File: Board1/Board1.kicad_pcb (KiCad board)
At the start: 2 copper layers, 100 x 62 mm, 60 parts, among them J1 240VAC, J2 PTC Plate, J3 Thermo, J4 Cool. Plate, J5 OLED, J6 Rotary Encoder, J7 ESPFlash, J8 Fan, J9 IR Therm, Q1 2N7002E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

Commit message: Resolve library and ERC issues
No changes to design.
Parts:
- U4: footprint Relay_THT:SSR_AQG22105 -> 0_Project:SSR_AQG22105
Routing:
- net GND: track 42.6 -> 43.9 mm, vias 33 -> 34
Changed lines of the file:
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@@
 	)
 	(paper "A4")
+	(title_block
+		(title "Board 1 (Reflow Controller)")
+		(date "2025-02-20")
+		(rev "1.1")
+		(company "Wattle Labs")
+	)
 	(layers
 		(0 "F.Cu" signal "Front")
@@
 	(net 52 "unconnected-(U1-IO37-Pad30)")
 	(net 53 "unconnected-(U1-IO4-Pad4)")
-	(net 54 "unconnected-(U3-DNC-Pad8)")
+	(net 54 "unconnected-(U3-NC-Pad8)")
 	(net 55 "unconnected-(U1-IO38-Pad31)")
 	(net 56 "unconnected-(U1-IO3-Pad15)")
@@
 			)
 		)
-		(property "Description" "Cold Junction K-type Termocouple Interface, SPI, SO8"
+		(property "Description" "Cold Junction K-type Thermocouple Interface, SPI, SOIC-8"
 			(at 0 0 0)
 			(layer "F.Fab")
@@
 			)
 		)
-		(property "Supplier" "https://www.digikey.co.nz/en/products/detail/analog-devices-inc-maxim-integrated/MAX31855KASA/2591564"
+		(property "Supplier" ""
 			(at 0 0 0)
 			(unlocked yes)
@@
 			)
 		)
-		(property "Digikey_PN" "MAX31855KASA+-ND"
+		(property "Digikey_PN" ""
 			(at 0 0 0)
 			(unlocked yes)
@@
 			(roundrect_rratio 0.25)
 			(net 33 "+3.3V")
-			(pinfunction "V_CC")
+			(pinfunction "V_{CC}")
 			(pintype "power_in")
 		)
@@
 			(layers "F.Cu" "F.Paste" "F.Mask")
 			(roundrect_rratio 0.25)
-			(net 54 "unconnected-(U3-DNC-Pad8)")
-			(pinfunction "DNC")
-			(pintype "passive+no_connect")
+			(net 54 "unconnected-(U3-NC-Pad8)")
+			(pinfunction "NC")
+			(pintype "no_connect")
 		)
 		(model "${KICAD8_3DMODEL_DIR}/Package_SO.3dshapes/SOIC-8_3.9x4.9mm_P1.27mm.wrl"
@@
 			(net 0)
 			(net_name "")
-			(layers "F&B.Cu")
+			(layers "F.Cu" "B.Cu")
 			(hatch full 0.508)
 			(connect_pads
@@
 		)
 	)
-	(footprint "Relay_THT:SSR_AQG22105"
+	(footprint "0_Project:SSR_AQG22105"
 		(layer "F.Cu")
 		(at 55.2 55.4 180)
 		(property "Reference" "U4"
-			(at 11.5 -3.5 0)
+			(at 11.5 -3.6 180)
 			(layer "F.SilkS")
 			(effects
@@
 		)
 		(property "Value" "AQG22205"
-			(at -3.61 4.135 0)
+			(at -3.61 4.135 180)
 			(layer "F.Fab")
 			(effects
@@
 			)
 		)
-		(property "Footprint" "Relay_THT:SSR_AQG22105"
-			(at 0 0 0)
+		(property "Footprint" "0_Project:SSR_AQG22105"
+			(at 0 0 180)
 			(layer "F.Fab")
 			(hide yes)
@@
 		)
 		(property "Datasheet" ""
-			(at 0 0 0)
+			(at 0 0 180)
 			(layer "F.Fab")
 			(hide yes)
@@
 		)
 		(property "Description" "SSR RELAY SPST-NO 2A 75-264V"
-			(at 0 0 0)
+			(at 0 0 180)
 			(layer "F.Fab")
 			(hide yes)
@@
 			(solder_mask_margin 0.102)
 		)
-		(model "${KIPRJMOD}/Library/3DModels/SSR_AQG22105.step"
-			(offset
-				(xyz 0 0 0)
-			)
-			(scale
-				(xyz 1 1 1)
-			)
-			(rotate
-				(xyz -90 0 0)
-			)
-		)
 	)
 	(footprint "Button_Switch_SMD:SW_SPST_PTS810"
@@
 			)
 		)
-		(property "Datasheet" "http://www.apem.com/int/index.php?controller=attachment&id_attachment=1371"
+		(property "Datasheet" "https://www.ckswitches.com/media/1476/pts810.pdf"
 			(at 0 0 180)
 			(unlocked yes)
@@
 			)
 		)
-		(property "Datasheet" "http://www.apem.com/int/index.php?controller=attachment&id_attachment=1371"
+		(property "Datasheet" "https://www.ckswitches.com/media/1476/pts810.pdf"
 			(at 0 0 180)
 			(unlocked yes)
@@
 		(attr through_hole)
 		(fp_line
-			(start -3.23 -3.38)
-			(end -3.23 33.860001)
+			(start 21.01 -3.38)
+			(end -3.23 -3.38)
 			(stroke
 				(width 0.12)
@@
 		)
 		(fp_line
-			(start 21.01 -3.379999)
-			(end -3.23 -3.38)
+			(start 21.01 -3.38)
+			(end 21.01 33.86)
 			(stroke
 				(width 0.12)
@@
 		)
 		(fp_line
-			(start 21.01 -3.379999)
-			(end 21.01 33.86)
+			(start -3.23 -3.38)
+			(end -3.23 33.86)
 			(stroke
 				(width 0.12)
@@
 		(fp_line
 			(start -3.61 -2)
-			(end -3.61 4.000001)
+			(end -3.61 4)
 			(stroke
 				(width 0.12)
@@
 		)
 		(fp_line
-			(start -3.23 33.860001)
+			(start -3.23 33.86)
 			(end 21.01 33.86)
 			(stroke
@@
 		)
 		(pad "3" thru_hole circle
-			(at 0 5.079999 90)
+			(at 0 5.08 90)
 			(size 2.3 2.3)
 			(drill 0.8)
@@
 	)
 	(segment
+		(start 118.575 78.825)
+		(end 118.55 78.85)
+		(width 0.2)
+		(layer "F.Cu")
+		(net 3)
+	)
+	(segment
+		(start 118.575 77.525)
+		(end 118.575 78.825)
+		(width 0.2)
+		(layer "F.Cu")
+		(net 3)
+	)
+	(segment
 		(start 123.35 46.6)
 		(end 123.35 48.35)
@@
 	)
 	(via
+		(at 118.55 78.85)
+		(size 0.6)
+		(drill 0.3)
+		(layers "F.Cu" "B.Cu")
+		(net 3)
+	)
+	(via
 		(at 73.75 55.331249)
 		(size 0.6)
@@
 		(net 32)
 		(net_name "+5V")
-		(layers "F&B.Cu")
+		(layers "F.Cu" "B.Cu")
 		(hatch edge 0.5)
 		(priority 1)
@@
 		(net 33)
 		(net_name "+3.3V")
-		(layers "F&B.Cu")
+		(layers "F.Cu" "B.Cu")
 		(hatch edge 0.5)
 		(priority 3)
@@
 		(net 3)
 		(net_name "GND")
-		(layers "F&B.Cu")
+		(layers "F.Cu" "B.Cu")
 		(hatch edge 0.5)
 		(priority 2)

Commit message: v1.2 release of board with bug fixes etc
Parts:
- removed C10: 10n, Capacitor_SMD:C_0603_1608Metric
- removed D2: 1N4148, Diode_SMD:Nexperia_CFP3_SOD-123W
- removed D3: SS15, Diode_SMD:D_SMA
- removed FB1, FB2: 470R 1LN, Resistor_SMD:R_0603_1608Metric
- removed J3: Thermo, Connector_PinHeader_2.54mm:PinHeader_1x02_P2.54mm_Vertical
- removed Q2: DMN3010LK3, Package_TO_SOT_SMD:TO-252-2
- removed R15: 4k7, Resistor_SMD:R_0603_1608Metric_Pad0.98x0.95mm_HandSolder
- removed R7, R8: 220R, Resistor_SMD:R_0603_1608Metric_Pad0.98x0.95mm_HandSolder
- removed R9: 10k, Resistor_SMD:R_0603_1608Metric_Pad0.98x0.95mm_HandSolder
- removed U5: VOS615A-1X001T, Package_SO:SSOP-4_4.4x2.6mm_P1.27mm
- added D4: SS15, Diode_SMD:D_SMA, F.Cu at (63.8, 71.6)
- added R12: 300, Resistor_SMD:R_0603_1608Metric, F.Cu at (92.0, 57.0)
- added U6: DMN3010LK3-13, Wattle_Mosfets:TO252-3L_DIO, F.Cu at (81.5, 54.5)
- C6: value 10u -> 22u
- C9: value 100n -> 0.1u
- J2: footprint TerminalBlock_Altech:Altech_AK100_1x02_P5.00mm -> TerminalBlock_Altech:Altech_AK100_1x03_P5.00mm
- J4: value Cool. Plate -> Cool.Plate
- J6: value Rotary Encoder -> Rot.Encoder
- J9: value IR Therm -> IRTherm
- U3: value MAX31855KASA -> DGD0280WT-7; footprint Package_SO:SOIC-8_3.9x4.9mm_P1.27mm -> Wattle_Mosfet_Drv:SOT23-5_INF
- U4: value AQG22205 -> AQG22105
- moved C9 17.8 mm to (96.8, 53.5), turned to 90 degrees
- moved U3 14.2 mm to (93.2, 53.0), turned to 180 degrees
- moved J2 5.00 mm to (37.2, 74.2)
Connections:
- C9 pad 1: +3.3V -> +5V
- J6 pad 3: ROTARY_SIG -> ROTARY_BTN
- J6 pad 5: ROTARY_BTN -> ROTARY_SIG
- U1 pad 20: THERMO_MISO -> unconnected-(U1-IO12-Pad20)
- U1 pad 21: THERMO_CS -> unconnected-(U1-IO13-Pad21)
- U1 pad 22: THERMO_SCK -> unconnected-(U1-IO14-Pad22)
- U1 pad 23: ROTARY_SIG -> ROTARY_BTN
- U1 pad 25: ROTARY_BTN -> ROTARY_SIG
- U3 pad 1: GND -> +5V
- U3 pad 2: Net-(U3-T-) -> GND
- U3 pad 3: Net-(U3-T+) -> FAN
- U3 pad 4: +3.3V -> unconnected-(U3-3V3-Pad4)
- U3 pad 5: THERMO_SCK -> Net-(U3-OUT)
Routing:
- net +5V: track 121.0 -> 133.4 mm
- net THERMO_SCK: track 10.0 -> 0.00 mm
- net THERMO_MISO: track 10.0 -> 0.00 mm
- net THERMO_CS: track 10.0 -> 0.00 mm
- net GND: track 43.9 -> 37.3 mm
- net +3.3V: track 133.9 -> 127.5 mm, vias 17 -> 16
- net ROTARY_BTN: track 28.3 -> 34.4 mm
- net ROTARY_SIG: track 34.4 -> 28.3 mm
- net Net-(D2-K): track 5.46 -> 0.00 mm
- net Net-(Q2-G): track 5.23 -> 0.00 mm
- net Net-(U3-T+): track 4.74 -> 0.00 mm
- net Net-(J2-Pin_1): track 22.5 -> 27.2 mm
- net Net-(U3-T-): track 4.62 -> 0.00 mm
- net Net-(U6-G): track 0.00 -> 4.38 mm
- net Net-(R7-Pad1): track 3.56 -> 0.00 mm
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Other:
- outline, holes or cut-outs redrawn
- board text added: "2025/03 - v1.2"
- board text added: "YAORP^{32}"
- board text removed: "2025/02 - v1.1"
- board text removed: "T+"
- board text removed: "T-"
- board text removed: "YAORP"

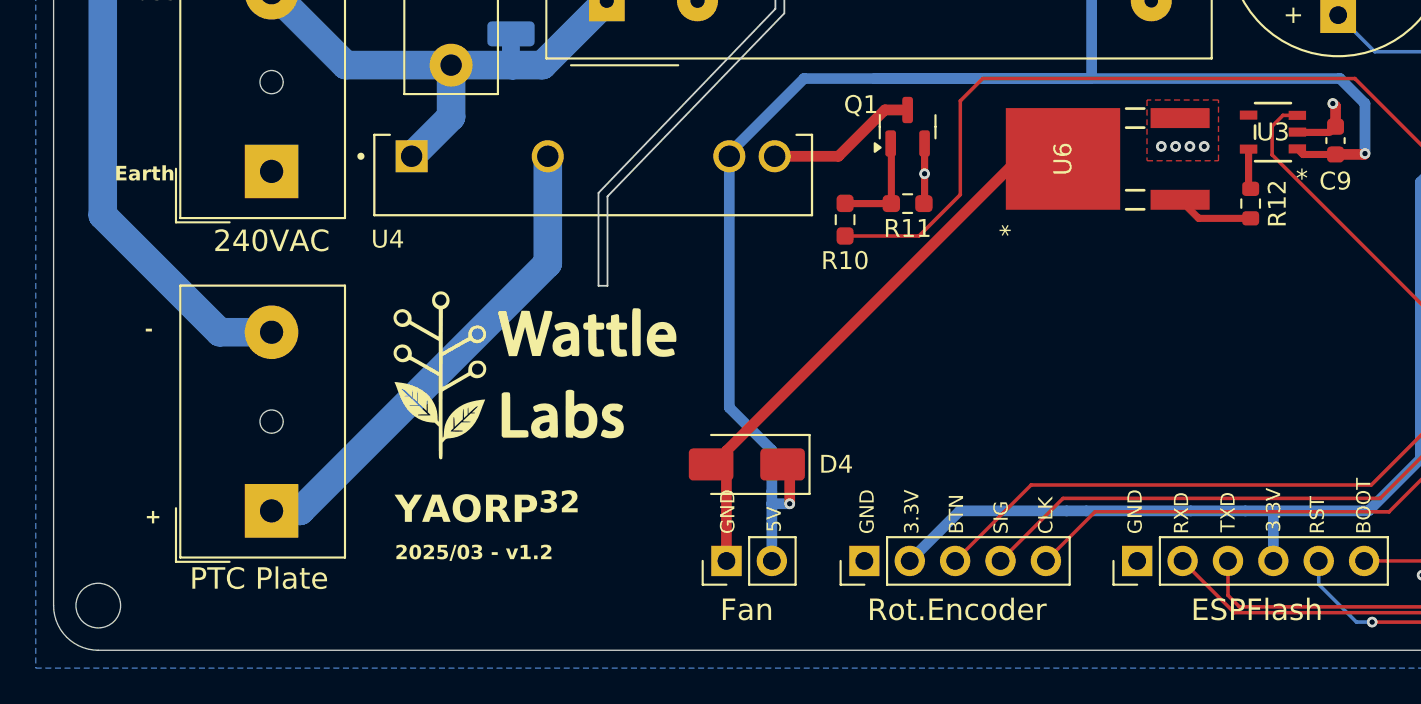
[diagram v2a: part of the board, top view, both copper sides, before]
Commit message: Tweaks to schematic for clarity and minor firmware
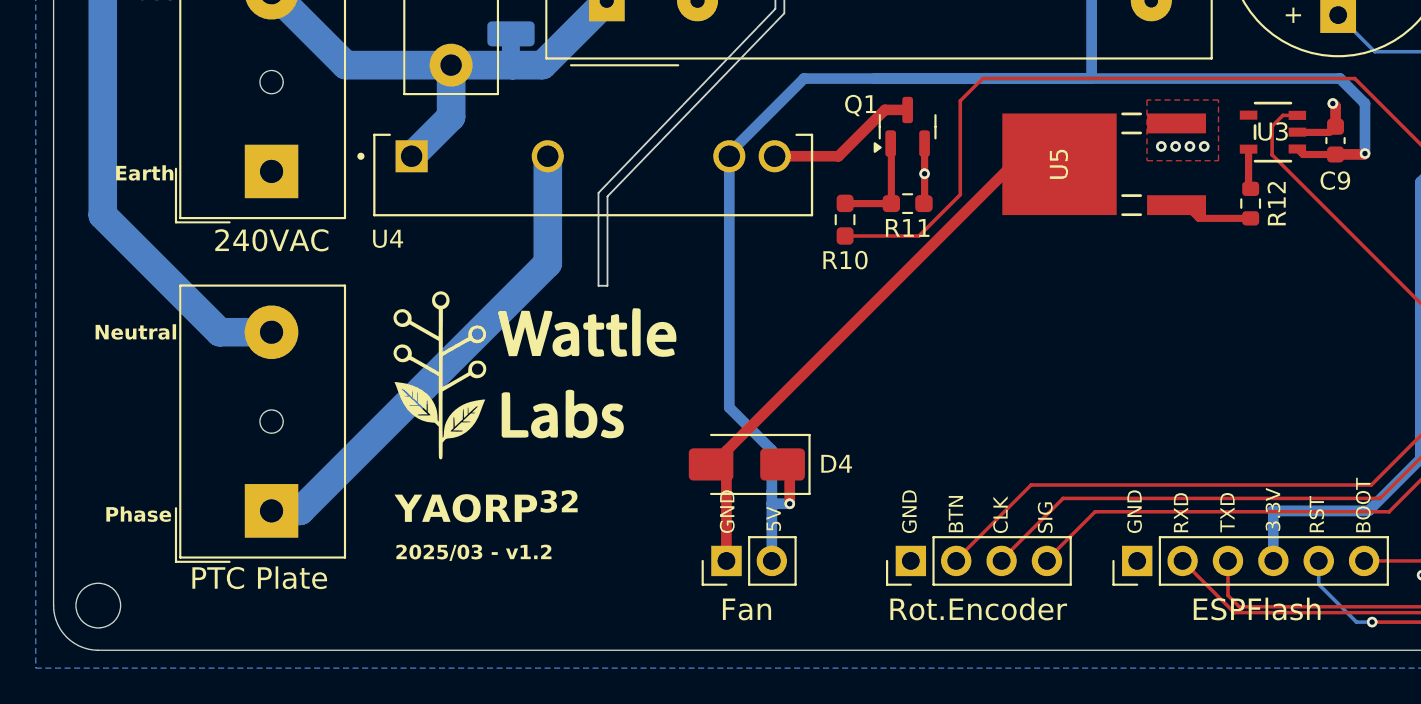
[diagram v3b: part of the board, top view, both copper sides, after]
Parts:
- removed U6: DMN3010LK3-13, Wattle_Mosfets:TO252-3L_DIO
- added U5: DMN3010LK3-13, Wattle_Mosfets:TO252-3L_DIO, F.Cu at (81.3, 54.8)
- C9: value 0.1u -> 100n
- D4: value SS15 -> SS12
- J6: footprint Connector_PinHeader_2.54mm:PinHeader_1x05_P2.54mm_Vertical -> Connector_PinHeader_2.54mm:PinHeader_1x04_P2.54mm_Vertical
- R12: value 300 -> 100
- moved J6 2.60 mm to (73.0, 77.0)
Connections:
- J6 pad 2: +3.3V -> ROTARY_BTN
- J6 pad 3: ROTARY_BTN -> ROTARY_CLK
- J6 pad 4: ROTARY_CLK -> ROTARY_SIG
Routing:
- net +3.3V: track 127.5 -> 105.9 mm
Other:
- board text removed: "+"
- board text removed: "-"
